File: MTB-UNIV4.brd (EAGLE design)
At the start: 100 x 80 mm, 25 parts, among them IC1 MEGA128-A, IC2 SN75176AP, IC3 NCP1117, SW1 FSMSM, X1 MKDSN1,5/4-5,08, X2 MKDSN1,5/4-5,08

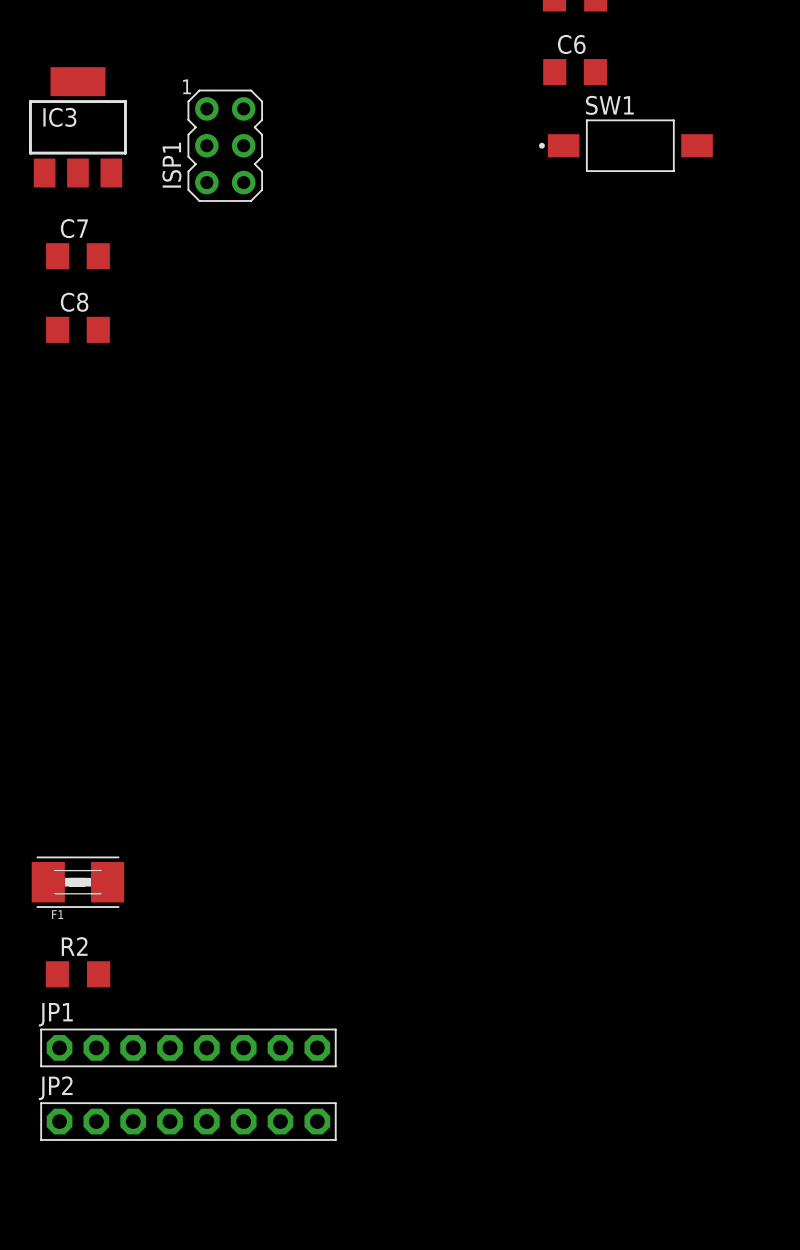
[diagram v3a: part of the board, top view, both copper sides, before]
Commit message: Vyměněno treset tlačítko za jumper
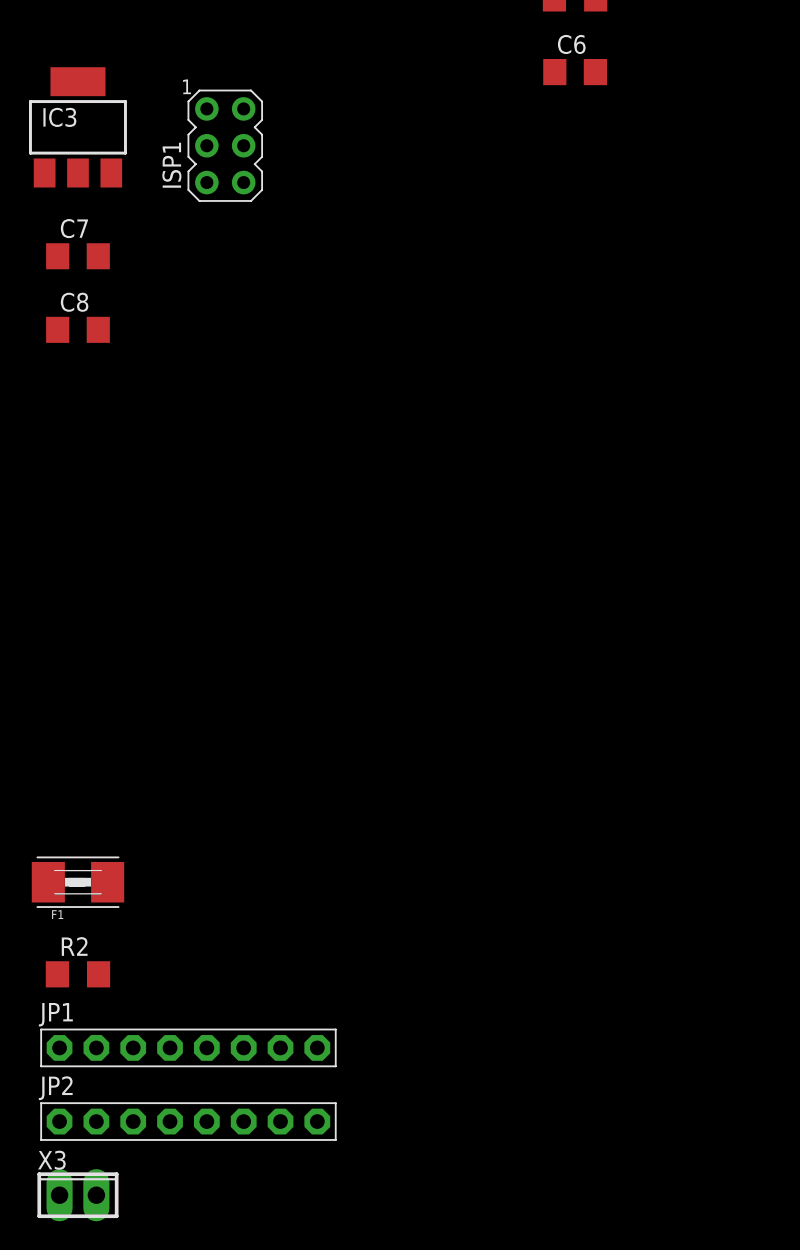
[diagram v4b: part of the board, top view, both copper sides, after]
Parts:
- removed SW1: FSMSM, Switch:FSMSM
- added X3: (no value), con-phoenix-254:2POL254
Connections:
- net GND: now also X3.1; no longer SW1.1
- net RST: now also X3.2; no longer SW1.2
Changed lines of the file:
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@@
 <?xml version="1.0" encoding="utf-8"?>
 <!DOCTYPE eagle SYSTEM "eagle.dtd">
-<eagle version="9.5.2">
+<eagle version="9.6.2">
 <drawing>
 <settings>
@@
 <attribute name="VALUE" x="-34.29" y="-110.49" size="1.27" layer="27"/>
 </element>
-<element name="SW1" library="Switch" library_urn="urn:adsk.eagle:library:11396471" package="FSMSM" package3d_urn="urn:adsk.eagle:package:12788211/3" value="FSMSM" x="-29.21" y="-113.03" smashed="yes">
-<attribute name="CREATED_BY" value=" PCBLayout.com" x="-29.21" y="-113.03" size="1.778" layer="27" display="off"/>
-<attribute name="DIGIKEY_PART_NUMBER" value="450-1140-ND" x="-29.21" y="-113.03" size="1.778" layer="27" display="off"/>
-<attribute name="MANUFACTURER" value="TE Connectivity ALCOSWITCH Switches" x="-29.21" y="-113.03" size="1.778" layer="27" display="off"/>
-<attribute name="MPN" value="FSMSM" x="-29.21" y="-113.03" size="1.778" layer="27" display="off"/>
-<attribute name="NAME" x="-32.370809375" y="-110.87945" size="1.27033125" layer="25"/>
-<attribute name="VALUE" x="-32.24706875" y="-116.6088" size="1.271709375" layer="27"/>
-</element>
 <element name="ISP1" library="adafruit" library_urn="urn:adsk.eagle:library:420" package="AVRISP" package3d_urn="urn:adsk.eagle:package:6240744/1" value="AVRISP-6" x="-57.15" y="-113.03" smashed="yes">
 <attribute name="NAME" x="-60.198" y="-116.078" size="1.27" layer="25" rot="R90"/>
@@
 <attribute name="NAME" x="-69.9262" y="-178.5112" size="1.27" layer="25" ratio="10"/>
 <attribute name="VALUE" x="-69.85" y="-183.515" size="1.27" layer="27"/>
+</element>
+<element name="X3" library="con-phoenix-254" library_urn="urn:adsk.eagle:library:172" package="2POL254" package3d_urn="urn:adsk.eagle:package:9320/1" value="" x="-67.31" y="-185.42" smashed="yes">
+<attribute name="MF" value="" x="-67.31" y="-185.42" size="1.778" layer="27" display="off"/>
+<attribute name="MPN" value="" x="-67.31" y="-185.42" size="1.778" layer="27" display="off"/>
+<attribute name="NAME" x="-70.104" y="-183.642" size="1.27" layer="25"/>
+<attribute name="OC_FARNELL" value="unknown" x="-67.31" y="-185.42" size="1.778" layer="27" display="off"/>
+<attribute name="OC_NEWARK" value="unknown" x="-67.31" y="-185.42" size="1.778" layer="27" display="off"/>
+<attribute name="POPULARITY" value="5" x="-67.31" y="-185.42" size="1.778" layer="27" display="off"/>
+<attribute name="VALUE" x="-70.104" y="-188.468" size="1.27" layer="27"/>
 </element>
 </elements>
@@
 <contactref element="C5" pad="2"/>
 <contactref element="C6" pad="2"/>
-<contactref element="SW1" pad="1"/>
 <contactref element="ISP1" pad="6"/>
 <contactref element="C7" pad="2"/>
@@
 <contactref element="C3" pad="2"/>
 <contactref element="X1" pad="4"/>
+<contactref element="X3" pad="1"/>
 <wire x1="-65.91" y1="-120.65" x2="-65.91" y2="-125.73" width="0" layer="19" extent="1-1"/>
 <wire x1="-69.61" y1="-114.91" x2="-65.91" y2="-120.65" width="0" layer="19" extent="1-1"/>
 <wire x1="-55.88" y1="-115.57" x2="-65.91" y2="-120.65" width="0" layer="19" extent="1-1"/>
-<wire x1="-33.81" y1="-113.03" x2="-55.88" y2="-115.57" width="0" layer="19" extent="1-1"/>
-<wire x1="-31.62" y1="-107.95" x2="-33.81" y2="-113.03" width="0" layer="19" extent="1-1"/>
+<wire x1="-31.62" y1="-107.95" x2="-55.88" y2="-115.57" width="0" layer="19" extent="1-1"/>
 <wire x1="-31.62" y1="-97.79" x2="-31.62" y2="-107.95" width="0" layer="19" extent="1-1"/>
 <wire x1="-31.62" y1="-92.71" x2="-31.62" y2="-97.79" width="0" layer="19" extent="1-1"/>
@@
 <wire x1="13.97" y1="-21.59" x2="13.97" y2="-17.78" width="0" layer="19" extent="1-1"/>
 <wire x1="13.97" y1="-29.21" x2="13.97" y2="-21.59" width="0" layer="19" extent="1-1"/>
-<wire x1="0" y1="-146.05" x2="-33.81" y2="-113.03" width="0" layer="19" extent="1-1"/>
+<wire x1="0" y1="-146.05" x2="-31.62" y2="-107.95" width="0" layer="19" extent="1-1"/>
+<wire x1="-68.58" y1="-185.42" x2="-65.91" y2="-125.73" width="0" layer="19" extent="1-1"/>
 </signal>
 <signal name="+5V">
@@
 <contactref element="C6" pad="1"/>
 <contactref element="IC1" pad="20"/>
-<contactref element="SW1" pad="2"/>
 <contactref element="ISP1" pad="5"/>
+<contactref element="X3" pad="2"/>
+<wire x1="-58.42" y1="-115.57" x2="-66.04" y2="-185.42" width="0" layer="19" extent="1-1"/>
 <wire x1="-34.42" y1="-107.95" x2="-58.42" y2="-115.57" width="0" layer="19" extent="1-1"/>
 <wire x1="-34.442" y1="-102.87" x2="-34.42" y2="-107.95" width="0" layer="19" extent="1-1"/>
-<wire x1="-24.61" y1="-113.03" x2="-34.42" y2="-107.95" width="0" layer="19" extent="1-1"/>
 <wire x1="-22.65" y1="-29.39" x2="-34.442" y2="-102.87" width="0" layer="19" extent="1-1"/>
 </signal>

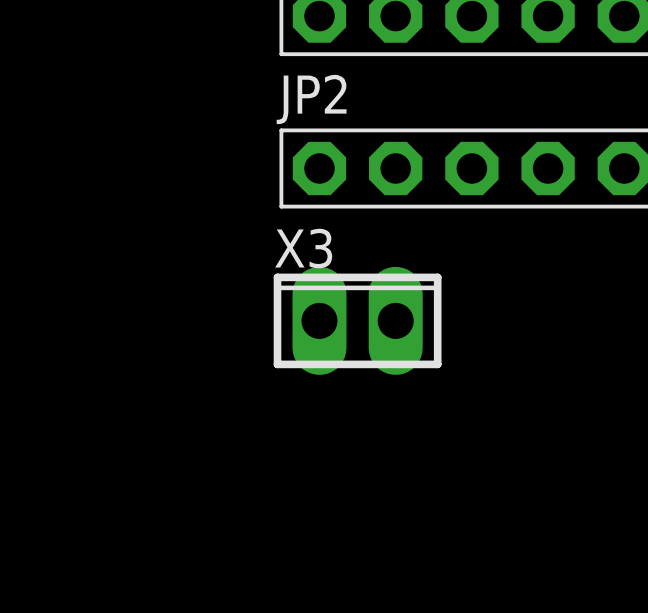
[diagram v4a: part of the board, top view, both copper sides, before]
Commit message: vloženy hodnoty k pasívním součástkám
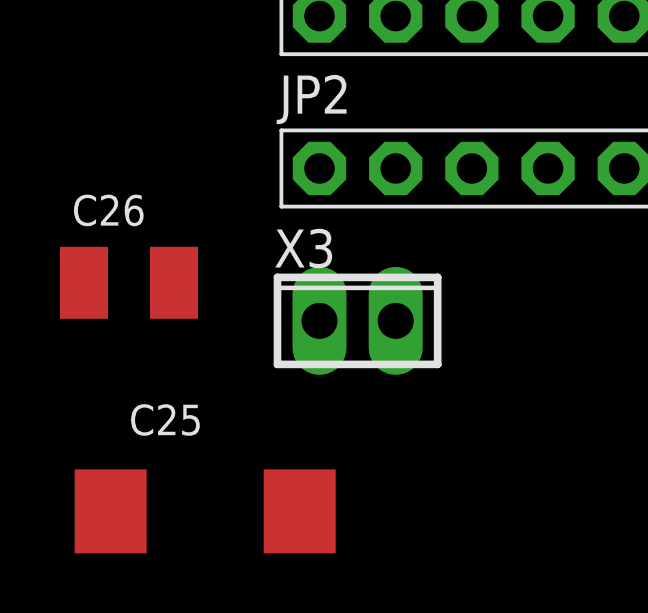
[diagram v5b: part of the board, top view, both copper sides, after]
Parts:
- added C25: 22uF, rcl:SMC_D
- added C26: 22uF, rcl:SMC_B
- C1, C2: value (none) -> 22pF
- C3, C4, C5, C6, C7, C8: value (none) -> 100nF
- R1: value (none) -> 10k
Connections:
- net +5V: now also C26.+
- net GND: now also C25.-, C26.-
- net N$13: now also C25.+
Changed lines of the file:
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@@
 <attribute name="VALUE" x="-25.4" y="-23.4823" size="1.27" layer="27"/>
 </element>
-<element name="C1" library="rcl" library_urn="urn:adsk.eagle:library:334" package="C1206" package3d_urn="urn:adsk.eagle:package:23618/2" value="" x="-24.13" y="-44.45" smashed="yes">
+<element name="C1" library="rcl" library_urn="urn:adsk.eagle:library:334" package="C1206" package3d_urn="urn:adsk.eagle:package:23618/2" value="22pF" x="-24.13" y="-44.45" smashed="yes">
 <attribute name="NAME" x="-25.4" y="-43.18" size="1.27" layer="25"/>
 <attribute name="POPULARITY" value="54" x="-24.13" y="-44.45" size="1.778" layer="27" display="off"/>
@@
 <attribute name="VALUE" x="-25.4" y="-46.99" size="1.27" layer="27"/>
 </element>
-<element name="C2" library="rcl" library_urn="urn:adsk.eagle:library:334" package="C1206" package3d_urn="urn:adsk.eagle:package:23618/2" value="" x="-24.13" y="-49.53" smashed="yes">
+<element name="C2" library="rcl" library_urn="urn:adsk.eagle:library:334" package="C1206" package3d_urn="urn:adsk.eagle:package:23618/2" value="22pF" x="-24.13" y="-49.53" smashed="yes">
 <attribute name="NAME" x="-25.4" y="-48.26" size="1.27" layer="25"/>
 <attribute name="POPULARITY" value="54" x="-24.13" y="-49.53" size="1.778" layer="27" display="off"/>
@@
 <attribute name="VALUE" x="-26.67" y="-75.565" size="1.27" layer="27"/>
 </element>
-<element name="C3" library="rcl" library_urn="urn:adsk.eagle:library:334" package="C1206" package3d_urn="urn:adsk.eagle:package:23618/2" value="" x="-33.02" y="-87.63" smashed="yes">
+<element name="C3" library="rcl" library_urn="urn:adsk.eagle:library:334" package="C1206" package3d_urn="urn:adsk.eagle:package:23618/2" value="100nF" x="-33.02" y="-87.63" smashed="yes">
 <attribute name="NAME" x="-34.29" y="-86.36" size="1.27" layer="25"/>
 <attribute name="POPULARITY" value="54" x="-33.02" y="-87.63" size="1.778" layer="27" display="off"/>
@@
 <attribute name="VALUE" x="-34.29" y="-90.17" size="1.27" layer="27"/>
 </element>
-<element name="C4" library="rcl" library_urn="urn:adsk.eagle:library:334" package="C1206" package3d_urn="urn:adsk.eagle:package:23618/2" value="" x="-33.02" y="-92.71" smashed="yes">
+<element name="C4" library="rcl" library_urn="urn:adsk.eagle:library:334" package="C1206" package3d_urn="urn:adsk.eagle:package:23618/2" value="100nF" x="-33.02" y="-92.71" smashed="yes">
 <attribute name="NAME" x="-34.29" y="-91.44" size="1.27" layer="25"/>
 <attribute name="POPULARITY" value="54" x="-33.02" y="-92.71" size="1.778" layer="27" display="off"/>
@@
 <attribute name="VALUE" x="-34.29" y="-95.25" size="1.27" layer="27"/>
 </element>
-<element name="C5" library="rcl" library_urn="urn:adsk.eagle:library:334" package="C1206" package3d_urn="urn:adsk.eagle:package:23618/2" value="" x="-33.02" y="-97.79" smashed="yes">
+<element name="C5" library="rcl" library_urn="urn:adsk.eagle:library:334" package="C1206" package3d_urn="urn:adsk.eagle:package:23618/2" value="100nF" x="-33.02" y="-97.79" smashed="yes">
 <attribute name="NAME" x="-34.29" y="-96.52" size="1.27" layer="25"/>
 <attribute name="POPULARITY" value="54" x="-33.02" y="-97.79" size="1.778" layer="27" display="off"/>
@@
 <attribute name="VALUE" x="-34.29" y="-100.33" size="1.27" layer="27"/>
 </element>
-<element name="R1" library="rcl" library_urn="urn:adsk.eagle:library:334" package="R1206" package3d_urn="urn:adsk.eagle:package:23540/2" value="" x="-33.02" y="-102.87" smashed="yes">
+<element name="R1" library="rcl" library_urn="urn:adsk.eagle:library:334" package="R1206" package3d_urn="urn:adsk.eagle:package:23540/2" value="10k" x="-33.02" y="-102.87" smashed="yes">
 <attribute name="NAME" x="-34.29" y="-101.6" size="1.27" layer="25"/>
 <attribute name="POPULARITY" value="41" x="-33.02" y="-102.87" size="1.778" layer="27" display="off"/>
@@
 <attribute name="VALUE" x="-34.29" y="-105.41" size="1.27" layer="27"/>
 </element>
-<element name="C6" library="rcl" library_urn="urn:adsk.eagle:library:334" package="C1206" package3d_urn="urn:adsk.eagle:package:23618/2" value="" x="-33.02" y="-107.95" smashed="yes">
+<element name="C6" library="rcl" library_urn="urn:adsk.eagle:library:334" package="C1206" package3d_urn="urn:adsk.eagle:package:23618/2" value="100nF" x="-33.02" y="-107.95" smashed="yes">
 <attribute name="NAME" x="-34.29" y="-106.68" size="1.27" layer="25"/>
 <attribute name="POPULARITY" value="54" x="-33.02" y="-107.95" size="1.778" layer="27" display="off"/>
@@
 <attribute name="VALUE" x="-69.85" y="-113.0808" size="1.27" layer="27"/>
 </element>
-<element name="C7" library="rcl" library_urn="urn:adsk.eagle:library:334" package="C1206" package3d_urn="urn:adsk.eagle:package:23618/2" value="" x="-67.31" y="-120.65" smashed="yes">
+<element name="C7" library="rcl" library_urn="urn:adsk.eagle:library:334" package="C1206" package3d_urn="urn:adsk.eagle:package:23618/2" value="100nF" x="-67.31" y="-120.65" smashed="yes">
 <attribute name="NAME" x="-68.58" y="-119.38" size="1.27" layer="25"/>
 <attribute name="POPULARITY" value="54" x="-67.31" y="-120.65" size="1.778" layer="27" display="off"/>
@@
 <attribute name="VALUE" x="-68.58" y="-123.19" size="1.27" layer="27"/>
 </element>
-<element name="C8" library="rcl" library_urn="urn:adsk.eagle:library:334" package="C1206" package3d_urn="urn:adsk.eagle:package:23618/2" value="" x="-67.31" y="-125.73" smashed="yes">
+<element name="C8" library="rcl" library_urn="urn:adsk.eagle:library:334" package="C1206" package3d_urn="urn:adsk.eagle:package:23618/2" value="100nF" x="-67.31" y="-125.73" smashed="yes">
 <attribute name="NAME" x="-68.58" y="-124.46" size="1.27" layer="25"/>
 <attribute name="POPULARITY" value="54" x="-67.31" y="-125.73" size="1.778" layer="27" display="off"/>
@@
 <attribute name="POPULARITY" value="5" x="-67.31" y="-185.42" size="1.778" layer="27" display="off"/>
 <attribute name="VALUE" x="-70.104" y="-188.468" size="1.27" layer="27"/>
+</element>
+<element name="C26" library="rcl" library_urn="urn:adsk.eagle:library:334" package="SMC_B" package3d_urn="urn:adsk.eagle:package:25920/5" value="22uF" x="-74.93" y="-184.15" smashed="yes">
+<attribute name="NAME" x="-76.835" y="-182.245" size="1.016" layer="25"/>
+<attribute name="POPULARITY" value="25" x="-74.93" y="-184.15" size="1.778" layer="27" display="off"/>
+<attribute name="SPICEPREFIX" value="C" x="-74.93" y="-184.15" size="1.778" layer="27" display="off"/>
+<attribute name="VALUE" x="-76.835" y="-186.69" size="1.016" layer="27"/>
+</element>
+<element name="C25" library="rcl" library_urn="urn:adsk.eagle:library:334" package="SMC_D" package3d_urn="urn:adsk.eagle:package:25923/2" value="22uF" x="-72.39" y="-191.77" smashed="yes">
+<attribute name="NAME" x="-74.93" y="-189.23" size="1.016" layer="25"/>
+<attribute name="POPULARITY" value="0" x="-72.39" y="-191.77" size="1.778" layer="27" display="off"/>
+<attribute name="SPICEPREFIX" value="C" x="-72.39" y="-191.77" size="1.778" layer="27" display="off"/>
+<attribute name="VALUE" x="-74.93" y="-195.58" size="1.016" layer="27"/>
 </element>
 </elements>
@@
 <contactref element="X1" pad="4"/>
 <contactref element="X3" pad="1"/>
+<contactref element="C25" pad="-"/>
+<contactref element="C26" pad="-"/>
 <wire x1="-65.91" y1="-120.65" x2="-65.91" y2="-125.73" width="0" layer="19" extent="1-1"/>
 <wire x1="-69.61" y1="-114.91" x2="-65.91" y2="-120.65" width="0" layer="19" extent="1-1"/>
@@
 <wire x1="13.97" y1="-29.21" x2="13.97" y2="-21.59" width="0" layer="19" extent="1-1"/>
 <wire x1="0" y1="-146.05" x2="-31.62" y2="-107.95" width="0" layer="19" extent="1-1"/>
-<wire x1="-68.58" y1="-185.42" x2="-65.91" y2="-125.73" width="0" layer="19" extent="1-1"/>
+<wire x1="-73.43" y1="-184.15" x2="-65.91" y2="-125.73" width="0" layer="19" extent="1-1"/>
+<wire x1="-68.58" y1="-185.42" x2="-73.43" y2="-184.15" width="0" layer="19" extent="1-1"/>
+<wire x1="-69.24" y1="-191.77" x2="-68.58" y2="-185.42" width="0" layer="19" extent="1-1"/>
 </signal>
 <signal name="+5V">
@@
 <contactref element="ISP1" pad="2"/>
 <contactref element="C3" pad="1"/>
+<contactref element="C26" pad="+"/>
 <wire x1="-67.31" y1="-114.91" x2="-68.71" y2="-125.73" width="0" layer="19" extent="1-1"/>
 <wire x1="-67.31" y1="-108.61" x2="-67.31" y2="-114.91" width="0" layer="19" extent="1-1"/>
@@
 <wire x1="-25.05" y1="-13.79" x2="-21.85" y2="-29.39" width="0" layer="19" extent="1-1"/>
 <wire x1="-15.45" y1="-13.79" x2="-25.05" y2="-13.79" width="0" layer="19" extent="1-1"/>
+<wire x1="-76.43" y1="-184.15" x2="-68.71" y2="-125.73" width="0" layer="19" extent="1-1"/>
 </signal>
 <signal name="MISO">
@@
 <contactref element="IC3" pad="3"/>
 <contactref element="D1" pad="C"/>
+<contactref element="C25" pad="+"/>
 <wire x1="-65.01" y1="-114.91" x2="-68.71" y2="-120.65" width="0" layer="19" extent="1-1"/>
+<wire x1="-75.54" y1="-191.77" x2="-68.71" y2="-120.65" width="0" layer="19" extent="1-1"/>
 <wire x1="-4.699" y1="-158.75" x2="-68.71" y2="-120.65" width="0" layer="19" extent="1-1"/>
 </signal>
